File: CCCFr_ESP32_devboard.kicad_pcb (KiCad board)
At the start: 2 copper layers, 54 x 85.6 mm, 75 parts, among them J1 USB_C_Receptacle_USB2.0_14P, J2 Conn_01x02_Pin, J3 Conn_01x18_Pin, J5 Conn_01x18_Pin, Q1 AO3401A, U1 ESP32-S3, U2 W25Q128JVS, U3 MCP73831-2-OT, U4 AMS1117-3.3, Y1 32.768 kHz, Y2 40MHz(10ppm)

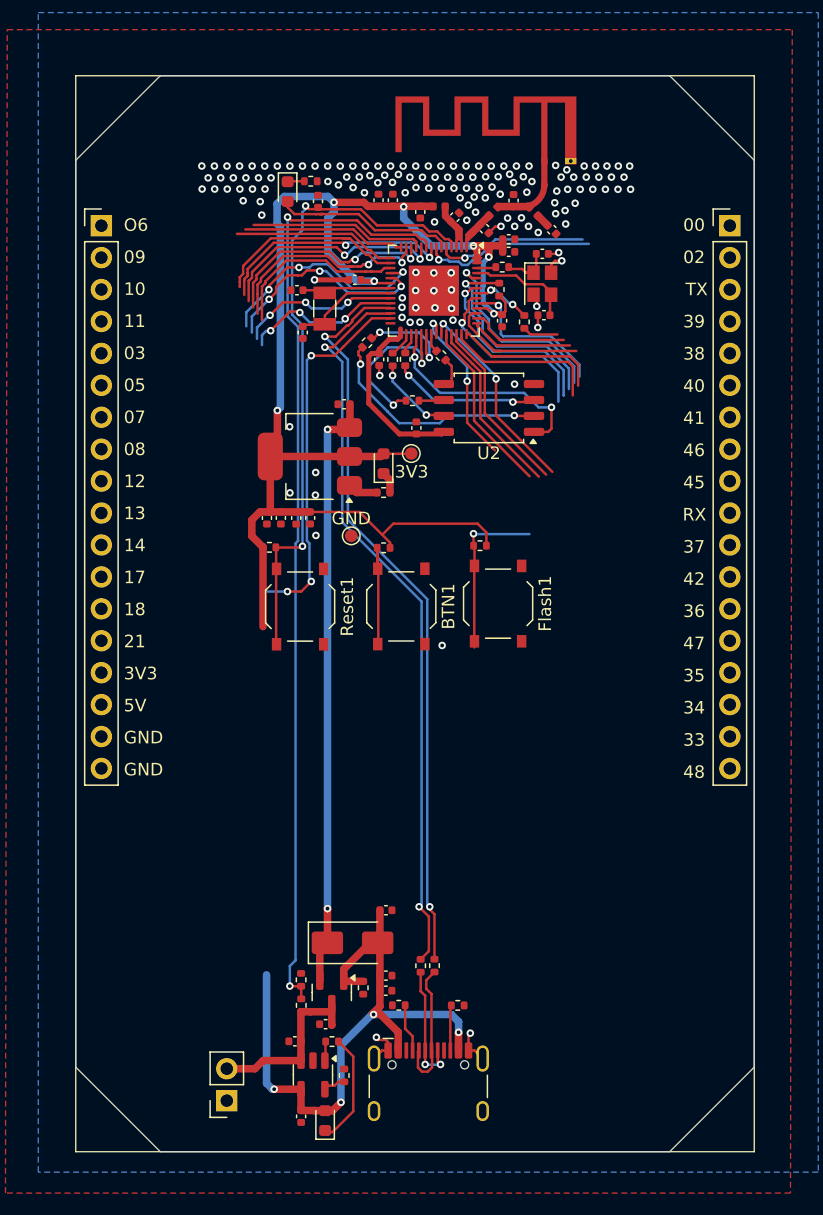
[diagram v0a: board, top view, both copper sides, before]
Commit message: integrated bottle opener
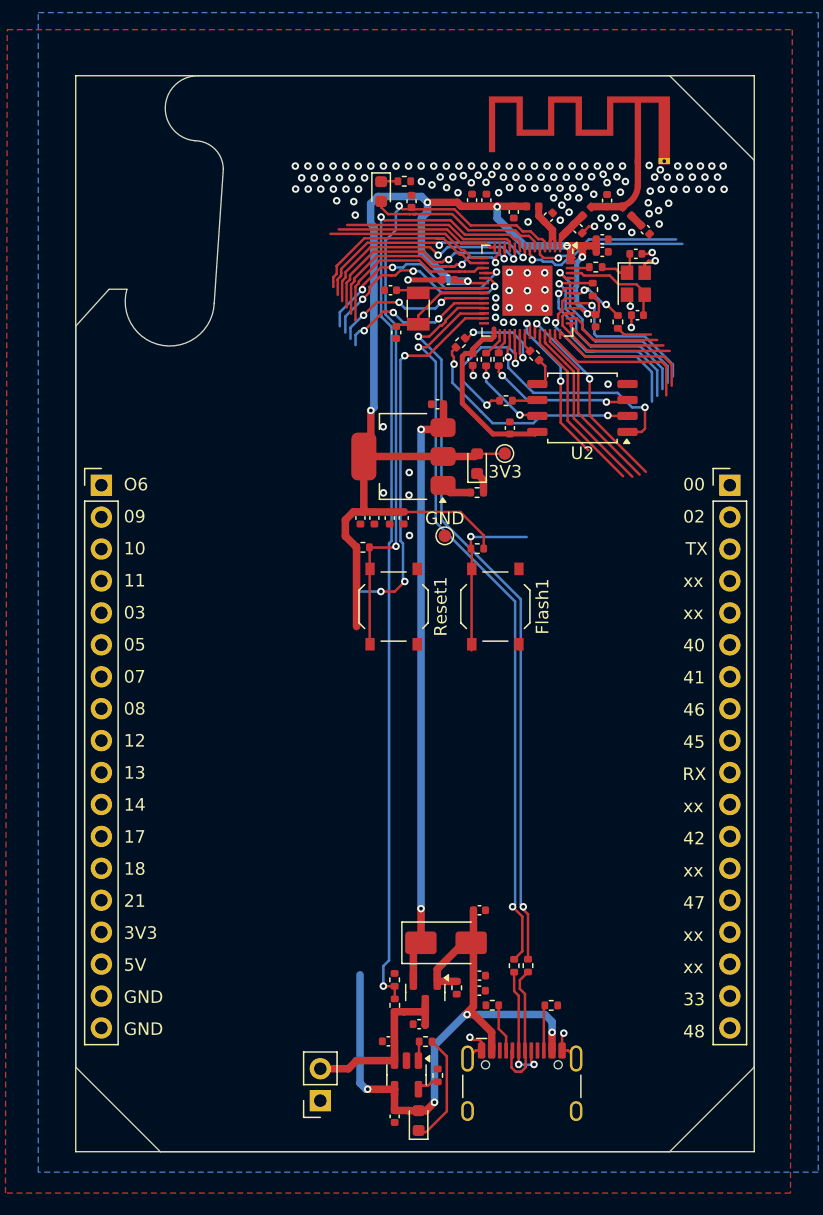
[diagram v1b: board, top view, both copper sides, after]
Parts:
- removed BTN1: BTN, Button_Switch_SMD:SW_Push_1P1T_XKB_TS-1187A
- removed R4: 10K, Resistor_SMD:R_0402_1005Metric
- moved J3 20.6 mm to (134.2, 69.1)
- moved J5 20.6 mm to (184.2, 69.1)
- moved C3 7.44 mm to (154.8, 71.8)
- moved D2 7.44 mm to (164.1, 67.4)
- moved R16 7.44 mm to (164.1, 69.7)
- moved R30 7.44 mm to (164.8, 59.1)
- moved U1 7.44 mm to (168.1, 53.7)
- moved 3V3 7.44 mm to (166.3, 66.6)
- moved AE1 7.44 mm to (176.9, 43.4)
- moved C10 7.44 mm to (161.8, 52.8)
- moved C11 7.44 mm to (173.5, 56.1)
- moved C13 7.44 mm to (163.8, 59.1)
- moved C14 7.44 mm to (177.5, 48.8)
- moved C15 7.44 mm to (158.9, 46.6)
- moved C16 7.44 mm to (164.3, 109.4)
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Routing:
- net VDD_CPU: track 116.0 -> 106.1 mm
- net IO14: track 25.5 -> 17.1 mm
- net GND: vias 143 -> 142
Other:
- outline, holes or cut-outs redrawn
- copper layers 2 -> 4
- board text added: "xx"
- board text removed: "34"
- board text removed: "35"
- board text removed: "36"
- board text removed: "37"
- board text removed: "38"
- board text removed: "39"

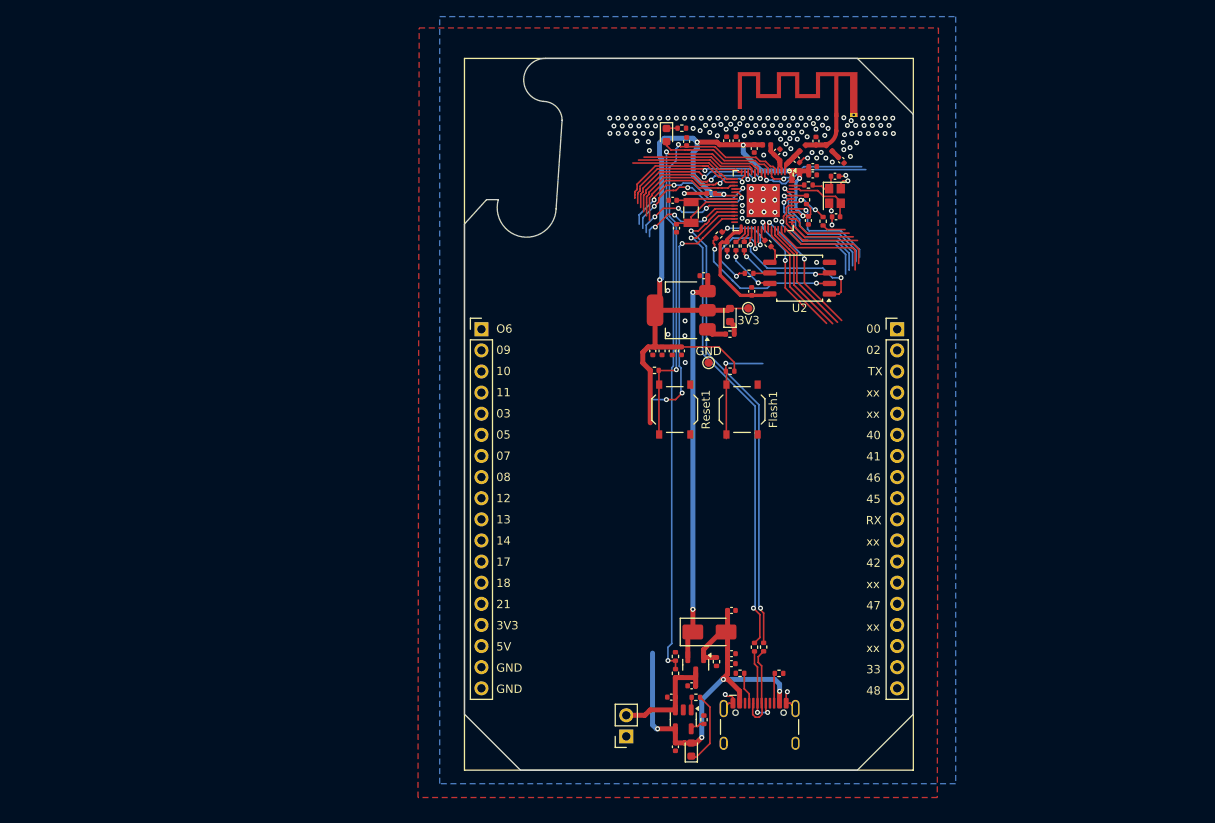
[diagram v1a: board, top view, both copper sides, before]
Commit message: Added 60 pieces of 2812B in the shape of CCCFr
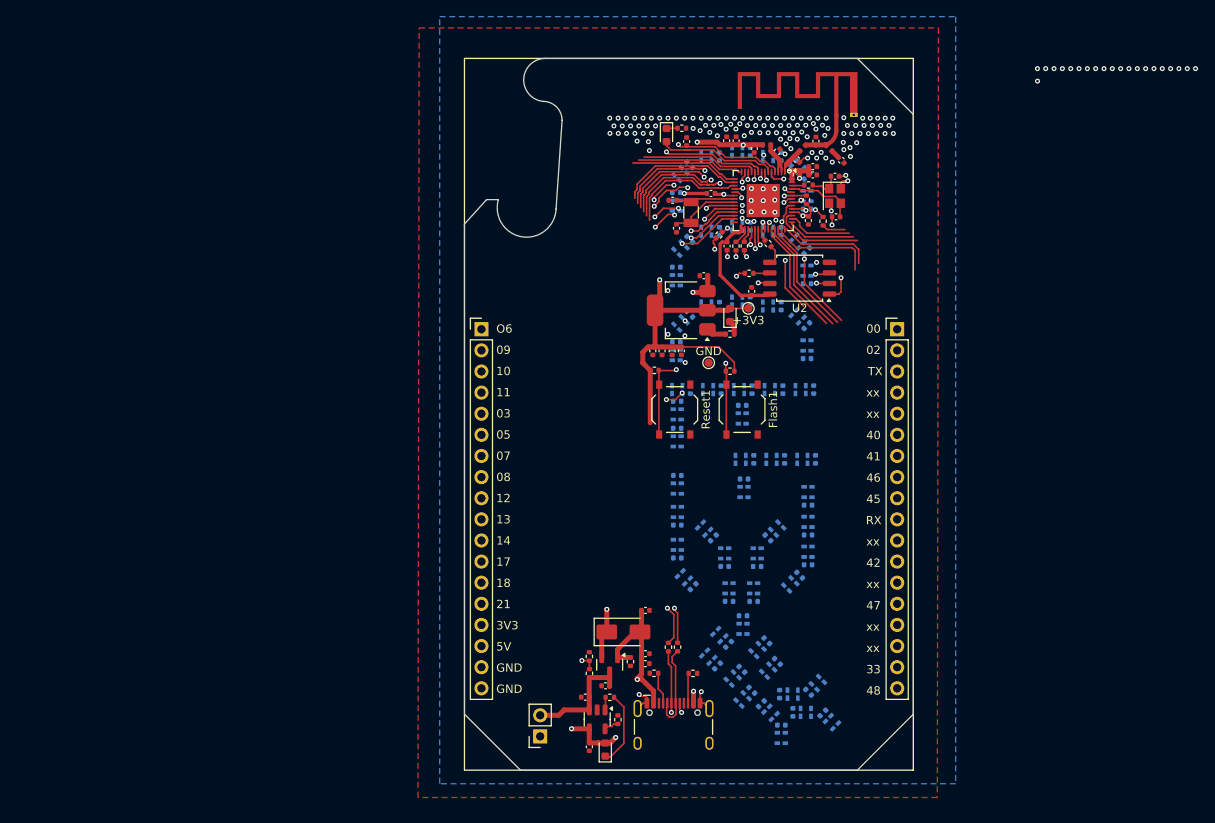
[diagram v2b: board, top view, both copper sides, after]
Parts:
- added C1: 0.1uF, Capacitor_SMD:C_0402_1005Metric, B.Cu at (162.8, 48.4)
- added C12: 0.1uF, Capacitor_SMD:C_0402_1005Metric, B.Cu at (159.3, 49.4)
- added C21: 0.1uF, Capacitor_SMD:C_0402_1005Metric, B.Cu at (173.4, 50.7)
- added C23: 0.1uF, Capacitor_SMD:C_0402_1005Metric, B.Cu at (157.7, 52.7)
- added C24: 0.1uF, Capacitor_SMD:C_0402_1005Metric, B.Cu at (173.4, 54.7)
- added C27: 0.1uF, Capacitor_SMD:C_0402_1005Metric, B.Cu at (162.8, 57.3)
- added C28: 0.1uF, Capacitor_SMD:C_0402_1005Metric, B.Cu at (166.6, 56.7)
- added C29: 0.1uF, Capacitor_SMD:C_0402_1005Metric, B.Cu at (170.3, 57.3)
- added C30: 0.1uF, Capacitor_SMD:C_0402_1005Metric, B.Cu at (159.3, 58.3)
- added C34: 0.1uF, Capacitor_SMD:C_0402_1005Metric, B.Cu at (173.4, 59.7)
- added C41: 0.1uF, Capacitor_SMD:C_0402_1005Metric, B.Cu at (157.7, 61.7)
- added C42: 0.1uF, Capacitor_SMD:C_0402_1005Metric, B.Cu at (173.4, 63.7)
- added C43: 0.1uF, Capacitor_SMD:C_0402_1005Metric, B.Cu at (162.8, 66.4)
- added C44: 0.1uF, Capacitor_SMD:C_0402_1005Metric, B.Cu at (166.6, 65.8)
- added C45: 0.1uF, Capacitor_SMD:C_0402_1005Metric, B.Cu at (170.3, 66.3)
- added C46: 0.1uF, Capacitor_SMD:C_0402_1005Metric, B.Cu at (159.3, 67.3)
- added C47: 0.1uF, Capacitor_SMD:C_0402_1005Metric, B.Cu at (173.4, 68.7)
- added C48: 0.1uF, Capacitor_SMD:C_0402_1005Metric, B.Cu at (157.7, 70.7)
- added C49: 0.1uF, Capacitor_SMD:C_0402_1005Metric, B.Cu at (173.4, 72.7)
- added C5: 0.1uF, Capacitor_SMD:C_0402_1005Metric, B.Cu at (166.6, 47.8)
- added C50: 0.1uF, Capacitor_SMD:C_0402_1005Metric, B.Cu at (159.3, 76.4)
- added C51: 0.1uF, Capacitor_SMD:C_0402_1005Metric, B.Cu at (163.1, 76.4)
- added C52: 0.1uF, Capacitor_SMD:C_0402_1005Metric, B.Cu at (166.8, 76.4)
- added C53: 0.1uF, Capacitor_SMD:C_0402_1005Metric, B.Cu at (170.5, 76.4)
- added C54: 0.1uF, Capacitor_SMD:C_0402_1005Metric, B.Cu at (174.2, 76.4)
- added C55: 0.1uF, Capacitor_SMD:C_0402_1005Metric, B.Cu at (157.8, 77.8)
- added C56: 0.1uF, Capacitor_SMD:C_0402_1005Metric, B.Cu at (165.6, 78.3)
- added C57: 0.1uF, Capacitor_SMD:C_0402_1005Metric, B.Cu at (157.8, 81.0)
- added C58: 0.1uF, Capacitor_SMD:C_0402_1005Metric, B.Cu at (167.0, 84.8)
- added C59: 0.1uF, Capacitor_SMD:C_0402_1005Metric, B.Cu at (170.7, 84.8)
- added C60: 0.1uF, Capacitor_SMD:C_0402_1005Metric, B.Cu at (174.4, 84.8)
- added C61: 0.1uF, Capacitor_SMD:C_0402_1005Metric, B.Cu at (157.8, 86.7)
- added C62: 0.1uF, Capacitor_SMD:C_0402_1005Metric, B.Cu at (165.8, 87.1)
- added C63: 0.1uF, Capacitor_SMD:C_0402_1005Metric, B.Cu at (173.5, 90.3)
- added C64: 0.1uF, Capacitor_SMD:C_0402_1005Metric, B.Cu at (157.8, 92.7)
- added C65: 0.1uF, Capacitor_SMD:C_0402_1005Metric, B.Cu at (162.1, 94.2)
- added C66: 0.1uF, Capacitor_SMD:C_0402_1005Metric, B.Cu at (168.7, 94.2)
- added C67: 0.1uF, Capacitor_SMD:C_0402_1005Metric, B.Cu at (173.5, 93.9)
- added C68: 0.1uF, Capacitor_SMD:C_0402_1005Metric, B.Cu at (157.8, 96.6)
- added C69: 0.1uF, Capacitor_SMD:C_0402_1005Metric, B.Cu at (163.5, 97.7)
- added C70: 0.1uF, Capacitor_SMD:C_0402_1005Metric, B.Cu at (167.4, 97.7)
- added C71: 0.1uF, Capacitor_SMD:C_0402_1005Metric, B.Cu at (173.5, 97.5)
- added C72: 0.1uF, Capacitor_SMD:C_0402_1005Metric, B.Cu at (159.7, 100.1)
- added C73: 0.1uF, Capacitor_SMD:C_0402_1005Metric, B.Cu at (164.0, 101.9)
- added C74: 0.1uF, Capacitor_SMD:C_0402_1005Metric, B.Cu at (167.0, 101.9)
- added C75: 0.1uF, Capacitor_SMD:C_0402_1005Metric, B.Cu at (172.5, 98.7)
- added C76: 0.1uF, Capacitor_SMD:C_0402_1005Metric, B.Cu at (165.7, 103.6)
- added C77: 0.1uF, Capacitor_SMD:C_0402_1005Metric, B.Cu at (168.5, 106.6)
- added C78: 0.1uF, Capacitor_SMD:C_0402_1005Metric, B.Cu at (162.6, 109.6)
- added C79: 0.1uF, Capacitor_SMD:C_0402_1005Metric, B.Cu at (165.5, 110.0)
- added C80: 0.1uF, Capacitor_SMD:C_0402_1005Metric, B.Cu at (166.7, 112.6)
- added C81: 0.1uF, Capacitor_SMD:C_0402_1005Metric, B.Cu at (169.8, 109.1)
- added C82: 0.1uF, Capacitor_SMD:C_0402_1005Metric, B.Cu at (170.1, 113.0)
- added C83: 0.1uF, Capacitor_SMD:C_0402_1005Metric, B.Cu at (173.6, 112.8)
- added C84: 0.1uF, Capacitor_SMD:C_0402_1005Metric, B.Cu at (167.9, 114.2)
- added C85: 0.1uF, Capacitor_SMD:C_0402_1005Metric, B.Cu at (171.7, 115.2)
- added C86: 0.1uF, Capacitor_SMD:C_0402_1005Metric, B.Cu at (170.3, 116.7)
- added C87: 0.1uF, Capacitor_SMD:C_0402_1005Metric, B.Cu at (175.3, 115.3)
- added C88: 0.1uF, Capacitor_SMD:C_0402_1005Metric, B.Cu at (163.9, 107.0)
- added C9: 0.1uF, Capacitor_SMD:C_0402_1005Metric, B.Cu at (170.3, 48.4)
- added D10: XL-1615RGBC-2812B, kustom:XL-1615RGBC-2812B, B.Cu at (157.7, 54.3)
- added D11: XL-1615RGBC-2812B, kustom:XL-1615RGBC-2812B, B.Cu at (173.4, 53.1)
- added D12: XL-1615RGBC-2812B, kustom:XL-1615RGBC-2812B, B.Cu at (161.3, 57.3)
- added D13: XL-1615RGBC-2812B, kustom:XL-1615RGBC-2812B, B.Cu at (165.0, 56.7)
- added D14: XL-1615RGBC-2812B, kustom:XL-1615RGBC-2812B, B.Cu at (168.7, 57.3)
- added D15: XL-1615RGBC-2812B, kustom:XL-1615RGBC-2812B, B.Cu at (158.2, 59.4)
- added D16: XL-1615RGBC-2812B, kustom:XL-1615RGBC-2812B, B.Cu at (172.2, 58.6)
- added D17: XL-1615RGBC-2812B, kustom:XL-1615RGBC-2812B, B.Cu at (157.7, 63.2)
- added D18: XL-1615RGBC-2812B, kustom:XL-1615RGBC-2812B, B.Cu at (173.4, 62.1)
- added D19: XL-1615RGBC-2812B, kustom:XL-1615RGBC-2812B, B.Cu at (161.3, 66.4)
- added D20: XL-1615RGBC-2812B, kustom:XL-1615RGBC-2812B, B.Cu at (165.0, 65.8)
- added D21: XL-1615RGBC-2812B, kustom:XL-1615RGBC-2812B, B.Cu at (168.7, 66.3)
- added D22: XL-1615RGBC-2812B, kustom:XL-1615RGBC-2812B, B.Cu at (158.2, 68.4)
- added D23: XL-1615RGBC-2812B, kustom:XL-1615RGBC-2812B, B.Cu at (172.2, 67.6)
- added D24: XL-1615RGBC-2812B, kustom:XL-1615RGBC-2812B, B.Cu at (157.7, 72.2)
- added D25: XL-1615RGBC-2812B, kustom:XL-1615RGBC-2812B, B.Cu at (173.4, 71.1)
- added D26: XL-1615RGBC-2812B, kustom:XL-1615RGBC-2812B, B.Cu at (157.8, 76.4)
- added D27: XL-1615RGBC-2812B, kustom:XL-1615RGBC-2812B, B.Cu at (161.5, 76.4)
- added D28: XL-1615RGBC-2812B, kustom:XL-1615RGBC-2812B, B.Cu at (165.2, 76.4)
- added D29: XL-1615RGBC-2812B, kustom:XL-1615RGBC-2812B, B.Cu at (168.9, 76.4)
- added D30: XL-1615RGBC-2812B, kustom:XL-1615RGBC-2812B, B.Cu at (172.6, 76.4)
- added D31: XL-1615RGBC-2812B, kustom:XL-1615RGBC-2812B, B.Cu at (157.8, 79.4)
- added D32: XL-1615RGBC-2812B, kustom:XL-1615RGBC-2812B, B.Cu at (165.6, 79.9)
- added D33: XL-1615RGBC-2812B, kustom:XL-1615RGBC-2812B, B.Cu at (157.8, 82.6)
- added D34: XL-1615RGBC-2812B, kustom:XL-1615RGBC-2812B, B.Cu at (165.4, 84.8)
- added D35: XL-1615RGBC-2812B, kustom:XL-1615RGBC-2812B, B.Cu at (169.1, 84.8)
- added D36: XL-1615RGBC-2812B, kustom:XL-1615RGBC-2812B, B.Cu at (172.8, 84.8)
- added D37: XL-1615RGBC-2812B, kustom:XL-1615RGBC-2812B, B.Cu at (157.8, 88.3)
- added D38: XL-1615RGBC-2812B, kustom:XL-1615RGBC-2812B, B.Cu at (165.8, 88.7)
- added D39: XL-1615RGBC-2812B, kustom:XL-1615RGBC-2812B, B.Cu at (173.5, 88.7)
- added D40: XL-1615RGBC-2812B, kustom:XL-1615RGBC-2812B, B.Cu at (157.8, 91.1)
- added D41: XL-1615RGBC-2812B, kustom:XL-1615RGBC-2812B, B.Cu at (161.0, 93.1)
- added D42: XL-1615RGBC-2812B, kustom:XL-1615RGBC-2812B, B.Cu at (169.8, 93.1)
- added D43: XL-1615RGBC-2812B, kustom:XL-1615RGBC-2812B, B.Cu at (173.5, 92.3)
- added D44: XL-1615RGBC-2812B, kustom:XL-1615RGBC-2812B, B.Cu at (157.8, 95.1)
- added D45: XL-1615RGBC-2812B, kustom:XL-1615RGBC-2812B, B.Cu at (163.5, 96.1)
- added D46: XL-1615RGBC-2812B, kustom:XL-1615RGBC-2812B, B.Cu at (167.4, 96.1)
- added D47: XL-1615RGBC-2812B, kustom:XL-1615RGBC-2812B, B.Cu at (173.5, 95.9)
- added D48: XL-1615RGBC-2812B, kustom:XL-1615RGBC-2812B, B.Cu at (158.6, 99.0)
- added D49: XL-1615RGBC-2812B, kustom:XL-1615RGBC-2812B, B.Cu at (164.0, 100.3)
- added D5: XL-1615RGBC-2812B, kustom:XL-1615RGBC-2812B, B.Cu at (161.3, 48.4)
- added D50: XL-1615RGBC-2812B, kustom:XL-1615RGBC-2812B, B.Cu at (167.0, 100.3)
- added D51: XL-1615RGBC-2812B, kustom:XL-1615RGBC-2812B, B.Cu at (171.4, 99.8)
- added D52: XL-1615RGBC-2812B, kustom:XL-1615RGBC-2812B, B.Cu at (165.7, 105.2)
- added D53: XL-1615RGBC-2812B, kustom:XL-1615RGBC-2812B, B.Cu at (162.8, 105.9)
- added D54: XL-1615RGBC-2812B, kustom:XL-1615RGBC-2812B, B.Cu at (167.4, 107.7)
- added D55: XL-1615RGBC-2812B, kustom:XL-1615RGBC-2812B, B.Cu at (161.5, 108.5)
- added D56: XL-1615RGBC-2812B, kustom:XL-1615RGBC-2812B, B.Cu at (164.4, 111.2)
- added D57: XL-1615RGBC-2812B, kustom:XL-1615RGBC-2812B, B.Cu at (165.6, 113.7)
- added D58: XL-1615RGBC-2812B, kustom:XL-1615RGBC-2812B, B.Cu at (168.7, 110.2)
- added D59: XL-1615RGBC-2812B, kustom:XL-1615RGBC-2812B, B.Cu at (171.7, 113.0)
- added D6: XL-1615RGBC-2812B, kustom:XL-1615RGBC-2812B, B.Cu at (165.0, 47.8)
- added D60: XL-1615RGBC-2812B, kustom:XL-1615RGBC-2812B, B.Cu at (174.7, 111.7)
- added D61: XL-1615RGBC-2812B, kustom:XL-1615RGBC-2812B, B.Cu at (169.0, 115.3)
- added D62: XL-1615RGBC-2812B, kustom:XL-1615RGBC-2812B, B.Cu at (173.2, 115.2)
- added D63: XL-1615RGBC-2812B, kustom:XL-1615RGBC-2812B, B.Cu at (170.3, 118.3)
- added D64: XL-1615RGBC-2812B, kustom:XL-1615RGBC-2812B, B.Cu at (176.4, 116.4)
- added D7: XL-1615RGBC-2812B, kustom:XL-1615RGBC-2812B, B.Cu at (168.7, 48.4)
- added D8: XL-1615RGBC-2812B, kustom:XL-1615RGBC-2812B, B.Cu at (158.2, 50.5)
- added D9: XL-1615RGBC-2812B, kustom:XL-1615RGBC-2812B, B.Cu at (172.3, 49.6)
- added G***: LOGO, kustom:cccfr, B.Cu at (168.2, 83.0)
- moved C2 10.4 mm to (146.7, 113.4)
- moved C22 10.4 mm to (153.9, 103.0)
- moved C36 10.4 mm to (147.2, 119.4)
- moved C6 10.4 mm to (153.9, 108.2)
- moved Q1 10.4 mm to (149.6, 109.5)
- moved R19 10.4 mm to (147.2, 108.5)
- moved R20 10.4 mm to (152.1, 109.1)
- moved C16 10.3 mm to (153.9, 109.4)
- moved C8 10.3 mm to (149.2, 112.0)
- moved D1 10.3 mm to (149.1, 119.7)
- moved D4 10.3 mm to (151.3, 105.5)
- moved J1 10.3 mm to (157.3, 117.9)
- moved J2 10.3 mm to (141.3, 118.1)
- moved R1 10.3 mm to (150.6, 116.1)
- moved R12 10.3 mm to (147.2, 110.5)
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- renumbered 3V3 to +3V3
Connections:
- J5 pad 11: IO37 -> unconnected-(J5-Pin_11-Pad11)
- J5 pad 13: IO36 -> unconnected-(J5-Pin_13-Pad13)
- J5 pad 15: IO35 -> unconnected-(J5-Pin_15-Pad15)
- J5 pad 16: IO34 -> unconnected-(J5-Pin_16-Pad16)
- J5 pad 4: IO39 -> unconnected-(J5-Pin_4-Pad4)
- J5 pad 5: IO38 -> unconnected-(J5-Pin_5-Pad5)
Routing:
- net IO4/BAT: track 76.0 -> 40.6 mm
- net USB_D+: track 69.0 -> 67.7 mm
- net Net-(D60-DOUT): track 0.00 -> 1.23 mm
- net GND: vias 142 -> 162

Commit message: Added buttons
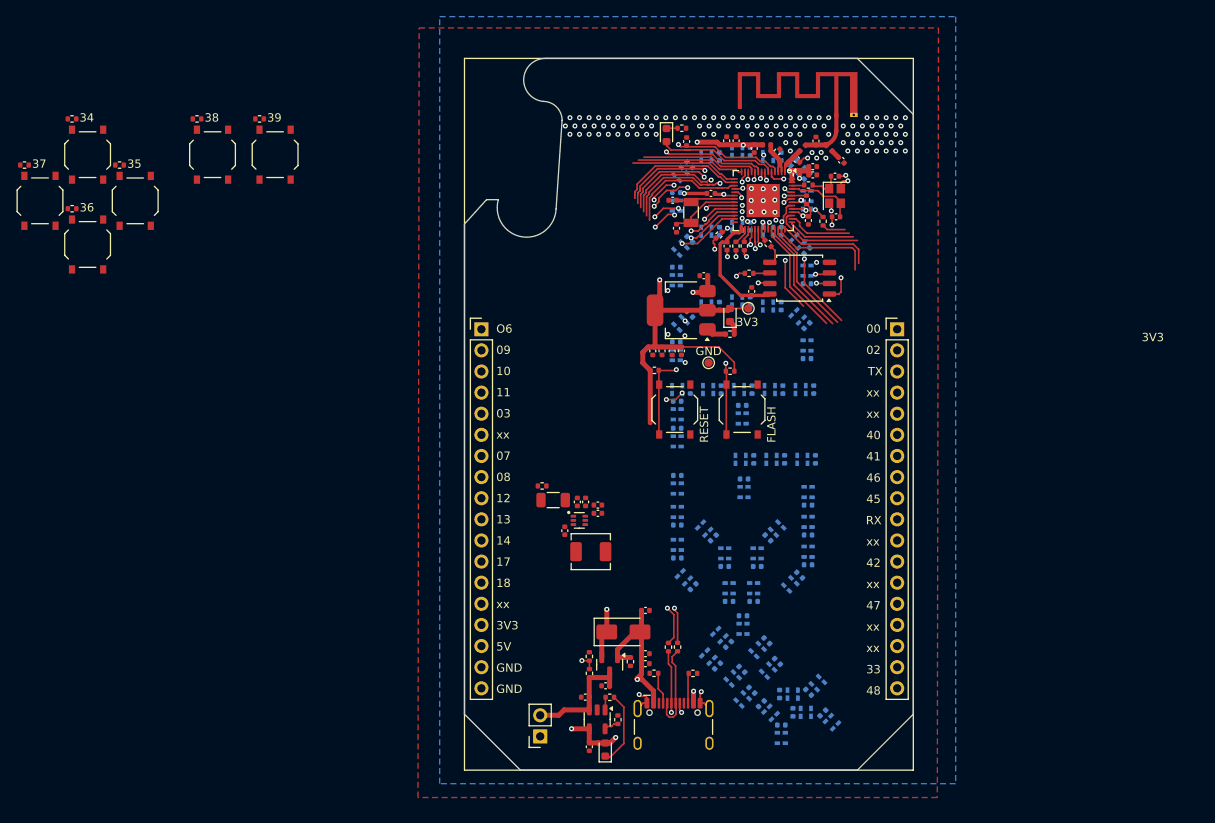
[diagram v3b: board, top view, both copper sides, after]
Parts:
- added BTN2: BTN, Button_Switch_SMD:SW_Push_1P1T_XKB_TS-1187A, F.Cu at (92.6, 53.7)
- added BTN3: BTN, Button_Switch_SMD:SW_Push_1P1T_XKB_TS-1187A, F.Cu at (86.9, 48.1)
- added BTN4: BTN, Button_Switch_SMD:SW_Push_1P1T_XKB_TS-1187A, F.Cu at (81.1, 53.7)
- added BTN5: BTN, Button_Switch_SMD:SW_Push_1P1T_XKB_TS-1187A, F.Cu at (86.9, 58.9)
- added BTN6: BTN, Button_Switch_SMD:SW_Push_1P1T_XKB_TS-1187A, F.Cu at (101.9, 48.1)
- added BTN7: BTN, Button_Switch_SMD:SW_Push_1P1T_XKB_TS-1187A, F.Cu at (109.4, 48.1)
- added C89: 10uF, Capacitor_SMD:C_0402_1005Metric, F.Cu at (144.2, 93.4)
- added C90: 10uF, Capacitor_SMD:C_0402_1005Metric, F.Cu at (145.8, 89.9)
- added C91: 10uF, Capacitor_SMD:C_0402_1005Metric, F.Cu at (146.7, 89.9)
- added C92: 10uF, Capacitor_SMD:C_0402_1005Metric, F.Cu at (148.2, 90.3)
- added C93: 10uF, Capacitor_SMD:C_0402_1005Metric, F.Cu at (148.2, 91.3)
- added L1: 1uH, Inductor_SMD:L_TechFuse_SL0420, F.Cu at (147.4, 95.9)
- added R10: 732K, Resistor_SMD:R_1206_3216Metric, F.Cu at (142.8, 89.7)
- added R3: 10K, Resistor_SMD:R_0402_1005Metric, F.Cu at (90.7, 49.4)
- added R4: 100K, Resistor_SMD:R_0402_1005Metric, F.Cu at (141.5, 88.0)
- added R5: 10K, Resistor_SMD:R_0402_1005Metric, F.Cu at (85.0, 43.8)
- added R6: 10K, Resistor_SMD:R_0402_1005Metric, F.Cu at (79.3, 49.4)
- added R7: 10K, Resistor_SMD:R_0402_1005Metric, F.Cu at (85.0, 54.6)
- added R8: 10K, Resistor_SMD:R_0402_1005Metric, F.Cu at (100.0, 43.8)
- added R9: 10K, Resistor_SMD:R_0402_1005Metric, F.Cu at (107.5, 43.8)
- added U5: TPS61023DRLR, PCM_SparkFun-Semiconductor-Standard:SOT-563, F.Cu at (146.0, 92.1)
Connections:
- D5 pad 2: unconnected-(D5-DIN-Pad2) -> IO21
- J3 pad 14: IO21 -> unconnected-(J3-Pin_14-Pad14)
- J3 pad 6: IO5 -> unconnected-(J3-Pin_6-Pad6)
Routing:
- net Net-(AE1-FEED): track 4.58 -> 4.50 mm, vias 0 -> 4
- net Net-(D3-K): vias 0 -> 3
- net Net-(C19-Pad1): vias 0 -> 2
- net Net-(C14-Pad1): vias 0 -> 4
- net GND: vias 162 -> 129
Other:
- board text added: "34"
- board text added: "35"
- board text added: "36"
- board text added: "37"
- board text added: "38"
- board text added: "39"
- board text added: "FLASH"
- board text added: "RESET"
- board text removed: "05"
- board text removed: "21"
